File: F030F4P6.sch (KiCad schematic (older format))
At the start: 7 parts, among them U1 STM32F030F4P6, Y1 Crystal

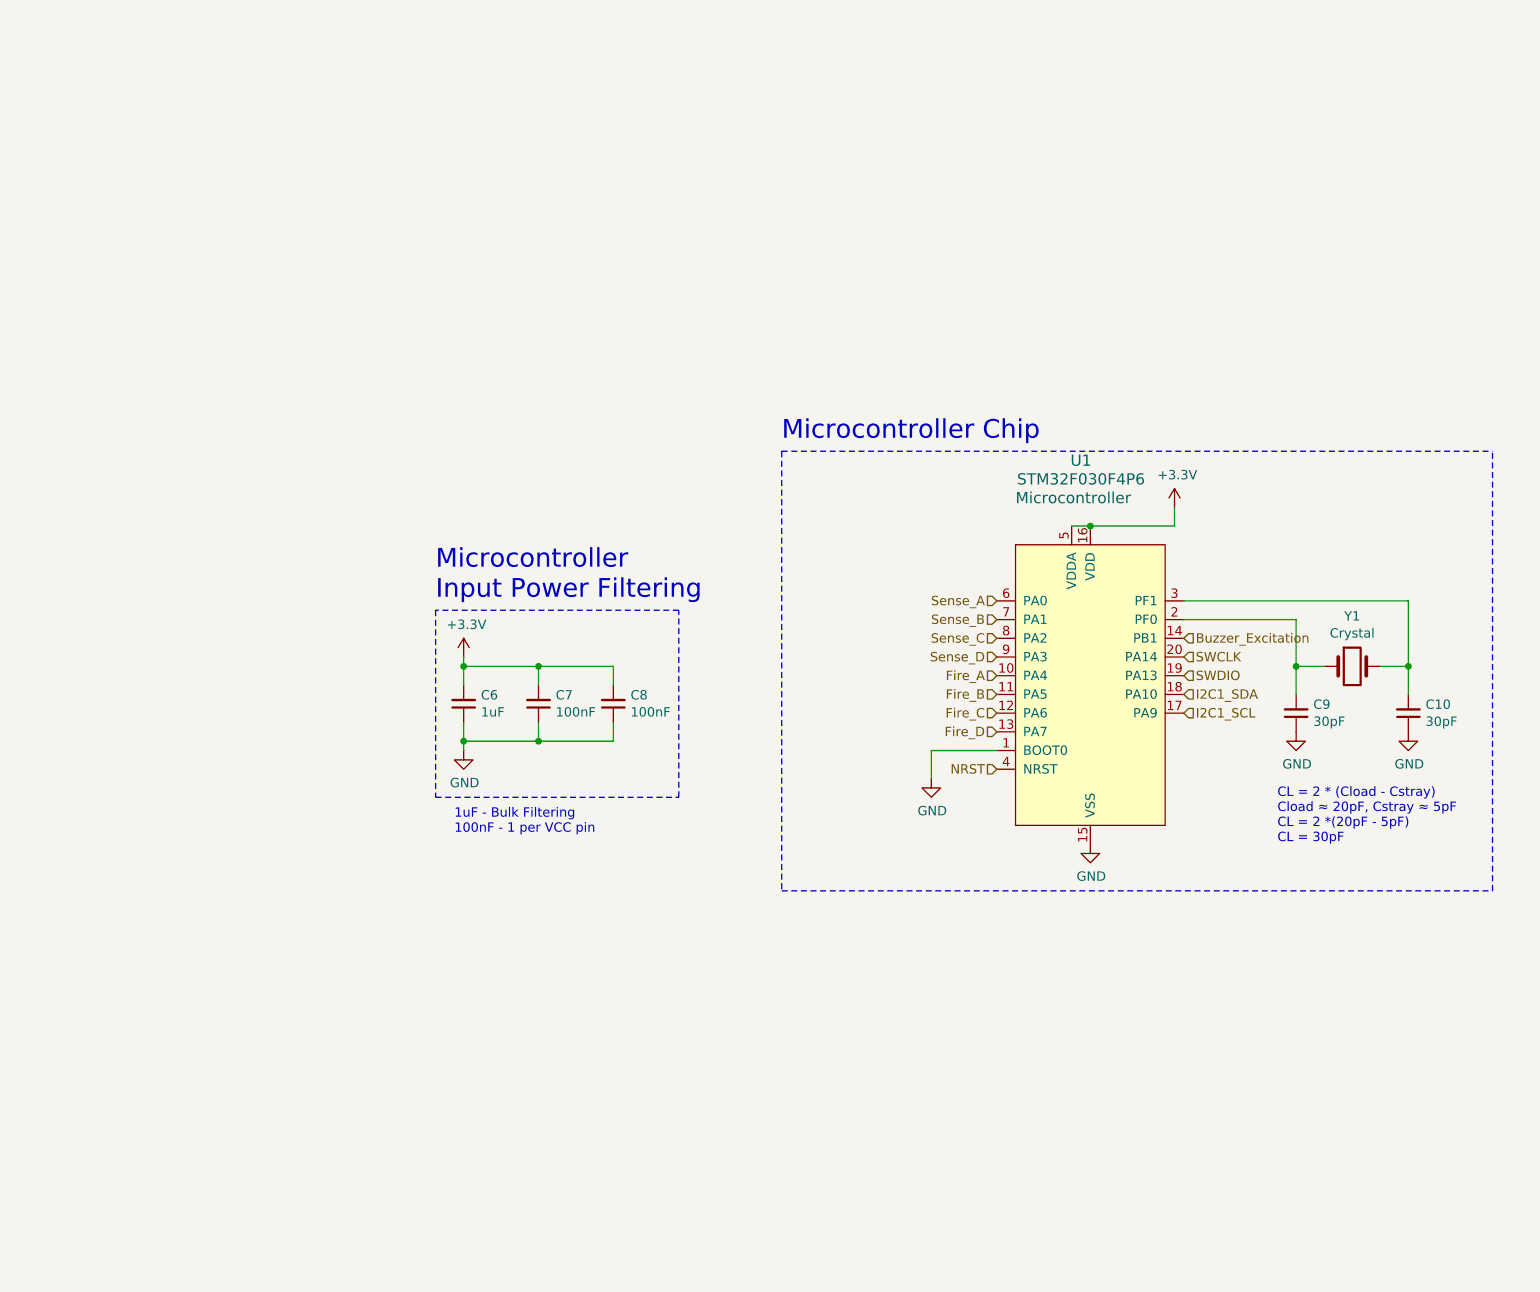
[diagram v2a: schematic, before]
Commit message: Updated PCB
Finalized most of the charges board and PCB
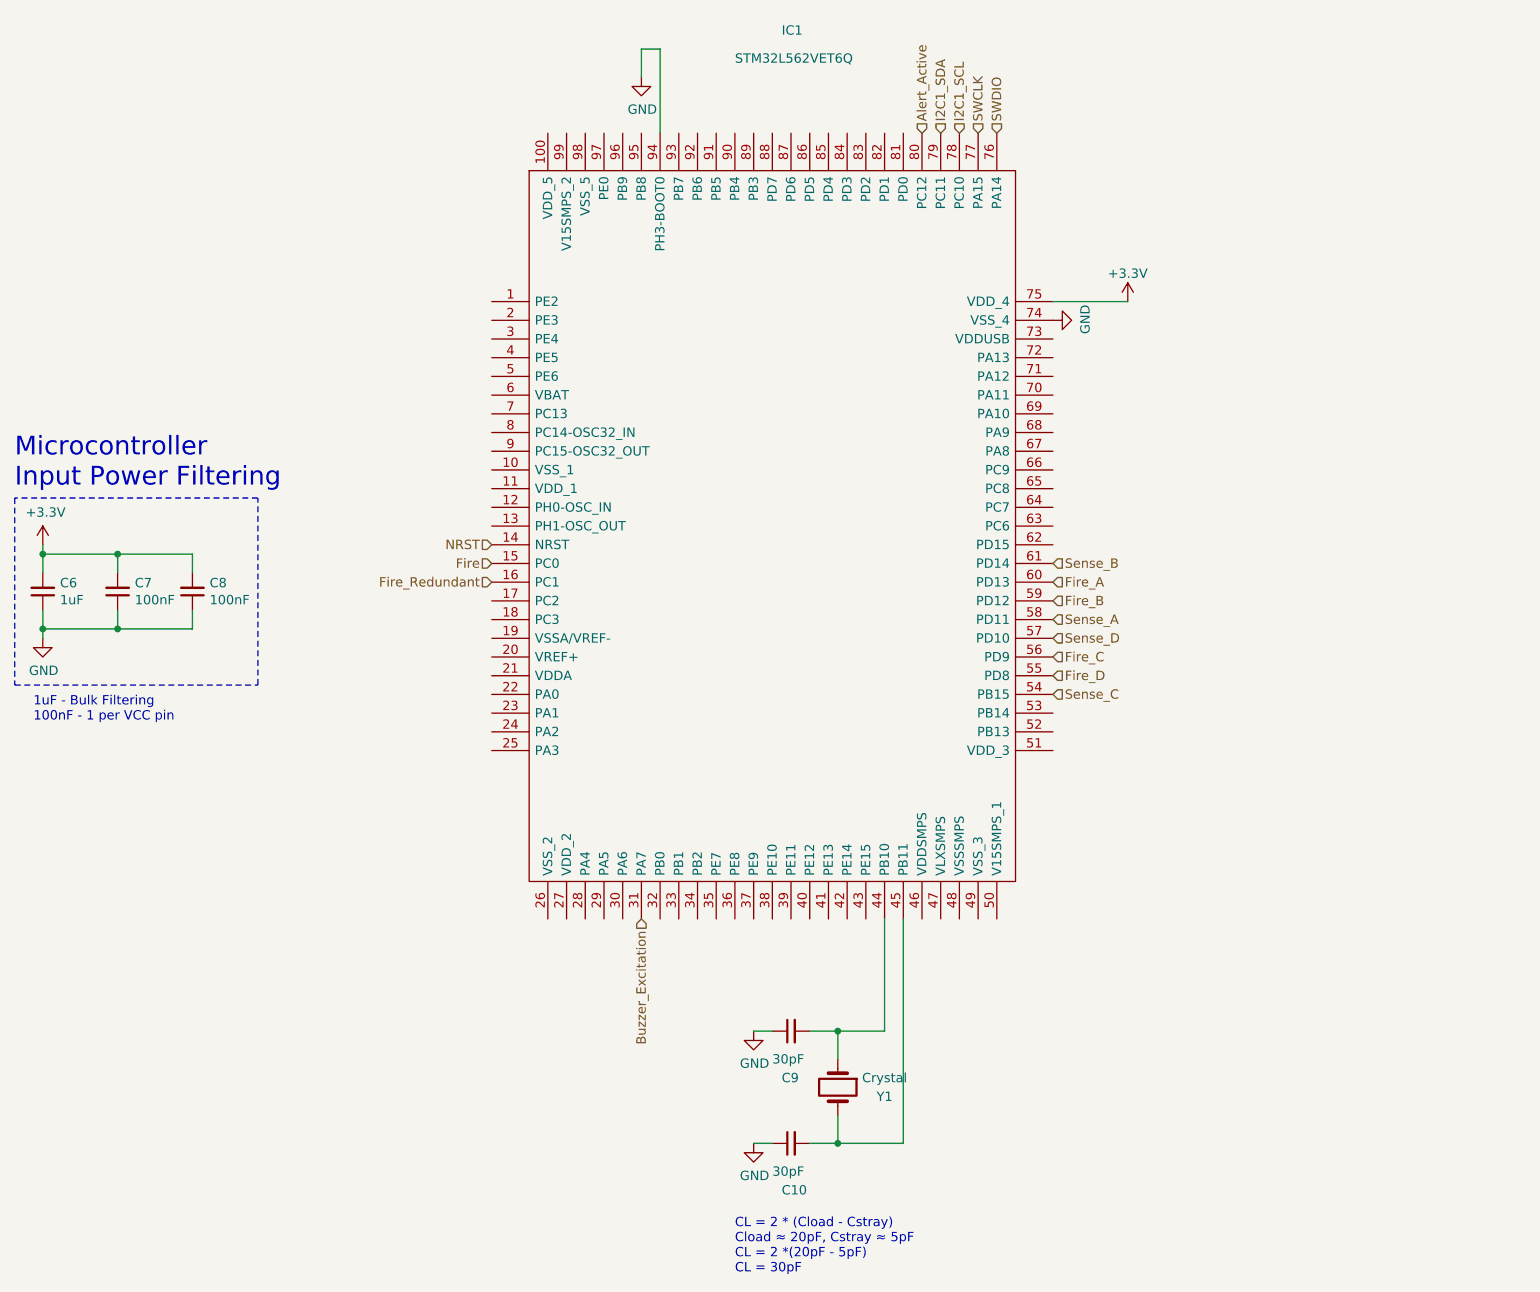
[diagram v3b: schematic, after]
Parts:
- removed U1: STM32F030F4P6, digikey-footprints:TSSOP-20_W4.4mm, symbol dk_Embedded-Microcontrollers:STM32F030F4P6
- added IC1: STM32L562VET6Q, SamacSys_Parts:QFP50P1600X1600X160-100N, symbol SamacSys_Parts:STM32L562VET6Q
- C10, C6, C7, C8, C9: footprint (none) -> Capacitor_SMD:C_0603_1608Metric
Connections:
- net +3V3: now also IC1.75 (VDD_4)
- net Buzzer_Excitation: now also IC1.31 (PA7)
- net Fire_A: now also IC1.60 (PD13)
- net Fire_B: now also IC1.59 (PD12)
- net Fire_C: now also IC1.56 (PD9)
- net Fire_D: now also IC1.55 (PD8)
- net GND: now also IC1.74 (VSS_4), IC1.94 (PH3-BOOT0)
- net I2C1_SCL: now also IC1.78 (PC10)
- net I2C1_SDA: now also IC1.79 (PC11)
- net NRST: now also IC1.14 (NRST)
- net SWCLK: now also IC1.77 (PA15)
- net SWDIO: now also IC1.76 (PA14)
- net Sense_A: now also IC1.58 (PD11)
- net Sense_B: now also IC1.61 (PD14)
- net Sense_C: now also IC1.54 (PB15)
- net Sense_D: now also IC1.57 (PD10)
- net at C9.2, Y1.1: now also IC1.44 (PB10)
- net at C10.2, Y1.2: now also IC1.45 (PB11)
- new net Alert_Active: IC1.80 (PC12)
- new net Fire: IC1.15 (PC0)
- new net Fire_Redundant: IC1.16 (PC1)
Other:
- note removed: "Microcontroller Chip"
- moved on the sheet: C10, C6, C7, C8, C9, Y1

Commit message: Fix to components
Changed the buzzer and terminal blocks
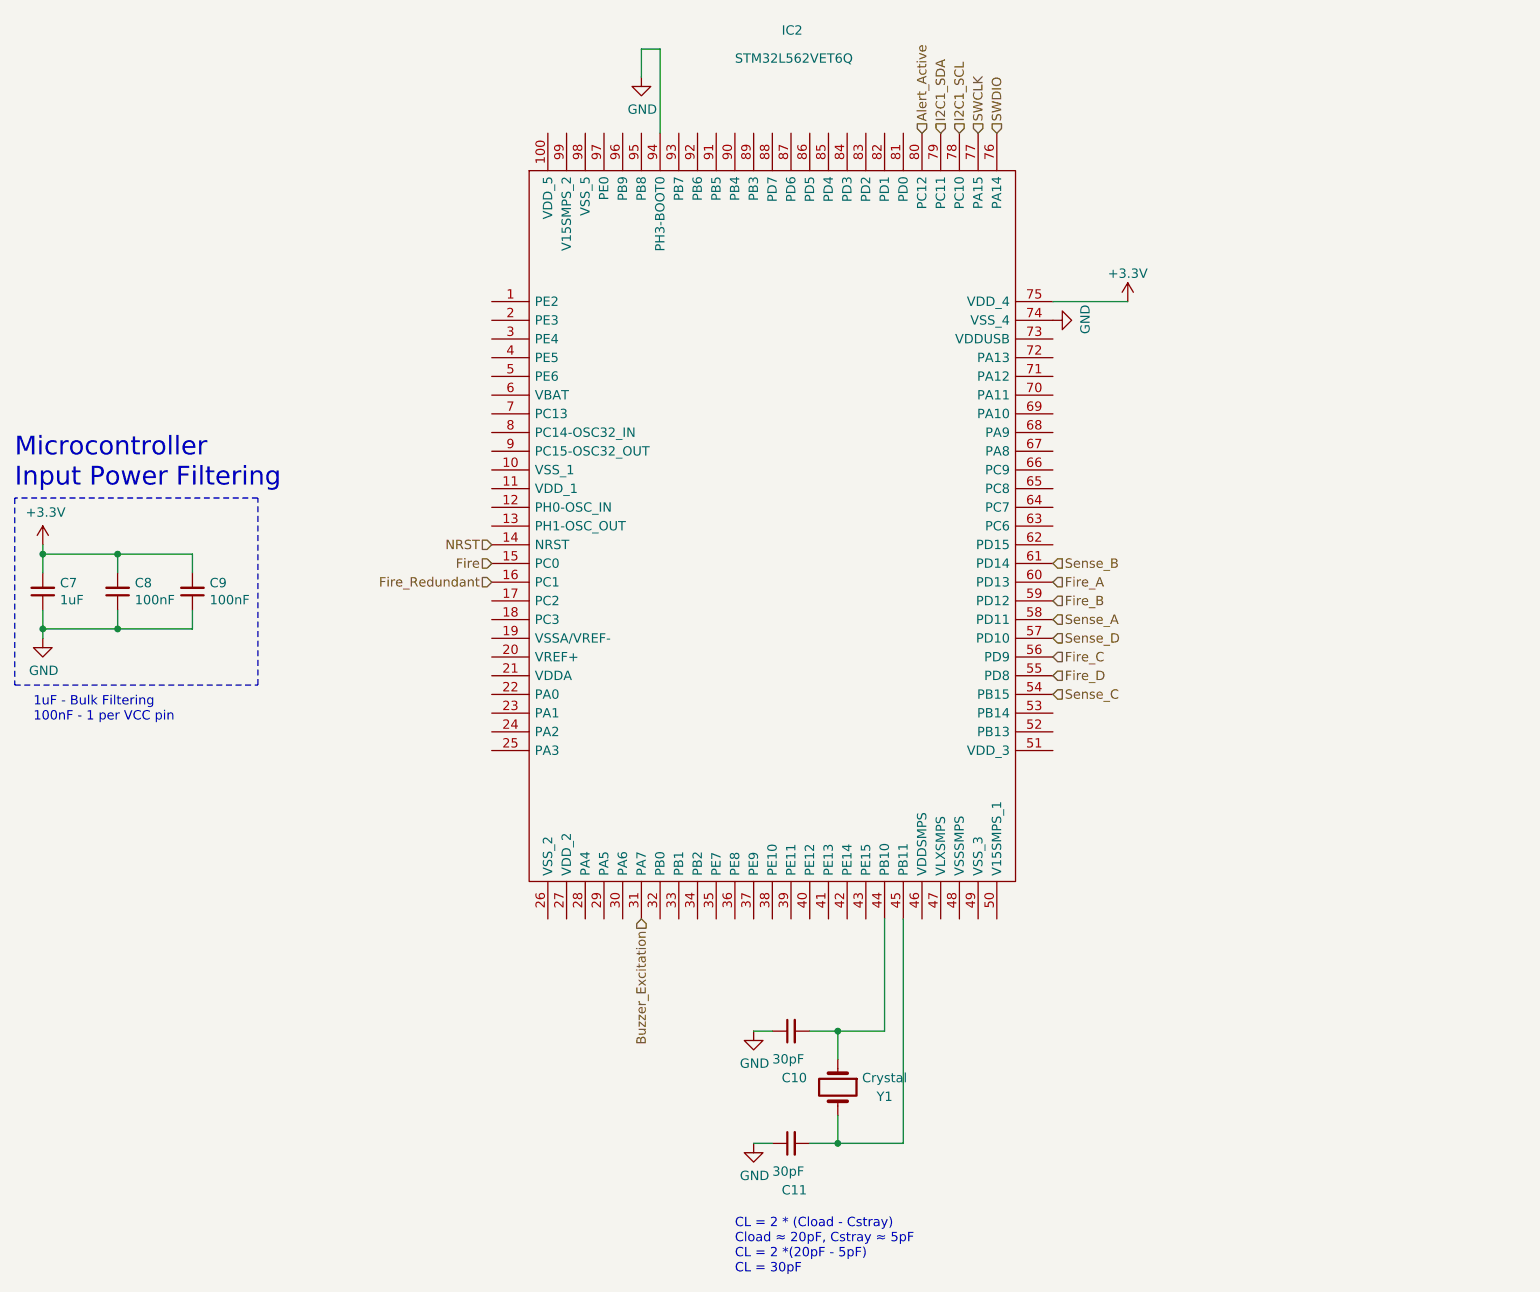
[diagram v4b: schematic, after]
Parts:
- renumbered C9 to C10, C10 to C11, C6 to C7, C7 to C8, C8 to C9, IC1 to IC2
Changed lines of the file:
@@
 P 5250 6700
 AR Path="/61614648" Ref="C?"  Part="1"
-AR Path="/6160DF75/61614648" Ref="C10"  Part="1"
-F 0 "C10" V 5000 6750 50  0000 R CNN
+AR Path="/6160DF75/61614648" Ref="C11"  Part="1"
+F 0 "C11" V 5000 6750 50  0000 R CNN
 F 1 "30pF" V 5100 6800 50  0000 R CNN
 F 2 "Capacitor_SMD:C_0603_1608Metric" H 5250 6700 50  0001 C CNN
@@
 P 5250 6100
 AR Path="/6161464E" Ref="C?"  Part="1"
-AR Path="/6160DF75/6161464E" Ref="C9"  Part="1"
-F 0 "C9" V 5000 6150 50  0000 R CNN
+AR Path="/6160DF75/6161464E" Ref="C10"  Part="1"
+F 0 "C10" V 5000 6150 50  0000 R CNN
 F 1 "30pF" V 5100 6200 50  0000 R CNN
 F 2 "Capacitor_SMD:C_0603_1608Metric" H 5250 6100 50  0001 C CNN
@@
 P 5050 6100
 AR Path="/61614655" Ref="#PWR?"  Part="1"
-AR Path="/6160DF75/61614655" Ref="#PWR037"  Part="1"
-F 0 "#PWR037" H 5050 5850 50  0001 C CNN
+AR Path="/6160DF75/61614655" Ref="#PWR035"  Part="1"
+F 0 "#PWR035" H 5050 5850 50  0001 C CNN
 F 1 "GND" H 5055 5927 50  0000 C CNN
 F 2 "" H 5050 6100 50  0001 C CNN
@@
 P 5050 6700
 AR Path="/6161465B" Ref="#PWR?"  Part="1"
-AR Path="/6160DF75/6161465B" Ref="#PWR038"  Part="1"
-F 0 "#PWR038" H 5050 6450 50  0001 C CNN
+AR Path="/6160DF75/6161465B" Ref="#PWR036"  Part="1"
+F 0 "#PWR036" H 5050 6450 50  0001 C CNN
 F 1 "GND" H 5055 6527 50  0000 C CNN
 F 2 "" H 5050 6700 50  0001 C CNN
@@
 P 1250 3750
 AR Path="/61614678" Ref="C?"  Part="1"
-AR Path="/6160DF75/61614678" Ref="C6"  Part="1"
-F 0 "C6" H 1158 3704 50  0000 R CNN
+AR Path="/6160DF75/61614678" Ref="C7"  Part="1"
+F 0 "C7" H 1158 3704 50  0000 R CNN
 F 1 "1uF" H 1158 3795 50  0000 R CNN
 F 2 "Capacitor_SMD:C_0603_1608Metric" H 1250 3750 50  0001 C CNN
@@
 P 1650 3750
 AR Path="/6161467E" Ref="C?"  Part="1"
-AR Path="/6160DF75/6161467E" Ref="C7"  Part="1"
-F 0 "C7" H 1558 3704 50  0000 R CNN
+AR Path="/6160DF75/6161467E" Ref="C8"  Part="1"
+F 0 "C8" H 1558 3704 50  0000 R CNN
 F 1 "100nF" H 1558 3795 50  0000 R CNN
 F 2 "Capacitor_SMD:C_0603_1608Metric" H 1650 3750 50  0001 C CNN
@@
 P 2050 3750
 AR Path="/61614684" Ref="C?"  Part="1"
-AR Path="/6160DF75/61614684" Ref="C8"  Part="1"
-F 0 "C8" H 1958 3704 50  0000 R CNN
+AR Path="/6160DF75/61614684" Ref="C9"  Part="1"
+F 0 "C9" H 1958 3704 50  0000 R CNN
 F 1 "100nF" H 1958 3795 50  0000 R CNN
 F 2 "Capacitor_SMD:C_0603_1608Metric" H 2050 3750 50  0001 C CNN
@@
 Wire Notes Line
 	1100 3250 1100 4250
-Text HLabel 6250 1300 1    50   Input ~ 0
-SWCLK
-Text HLabel 6350 1300 1    50   Input ~ 0
-SWDIO
 Text HLabel 6150 1300 1    50   Input ~ 0
 I2C1_SCL
@@
 I2C1_SDA
 $Comp
-L SamacSys_Parts:STM32L562VET6Q IC1
+L SamacSys_Parts:STM32L562VET6Q IC2
 U 1 1 61A3157F
 P 3650 2200
-F 0 "IC1" H 5200 3650 50  0000 L CNN
+F 0 "IC2" H 5200 3650 50  0000 L CNN
 F 1 "STM32L562VET6Q" H 4950 3500 50  0000 L CNN
 F 2 "SamacSys_Parts:QFP50P1600X1600X160-100N" H 6500 2900 50  0001 L CNN
@@
 P 6650 2300
 AR Path="/6161462F" Ref="#PWR?"  Part="1"
-AR Path="/6160DF75/6161462F" Ref="#PWR035"  Part="1"
-F 0 "#PWR035" H 6650 2050 50  0001 C CNN
+AR Path="/6160DF75/6161462F" Ref="#PWR037"  Part="1"
+F 0 "#PWR037" H 6650 2050 50  0001 C CNN
 F 1 "GND" H 6655 2127 50  0000 C CNN
 F 2 "" H 6650 2300 50  0001 C CNN
@@
 P 7050 2200
 AR Path="/6161463B" Ref="#PWR?"  Part="1"
-AR Path="/6160DF75/6161463B" Ref="#PWR036"  Part="1"
-F 0 "#PWR036" H 7050 2050 50  0001 C CNN
+AR Path="/6160DF75/6161463B" Ref="#PWR038"  Part="1"
+F 0 "#PWR038" H 7050 2050 50  0001 C CNN
 F 1 "+3.3V" H 7050 2350 50  0000 C CNN
 F 2 "" H 7050 2200 50  0001 C CNN
@@
 Text HLabel 6650 3900 2    50   Input ~ 0
 Sense_A
+Text HLabel 6250 1300 1    50   Input ~ 0
+SWCLK
+Text HLabel 6350 1300 1    50   Input ~ 0
+SWDIO
 $EndSCHEMATC

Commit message: updated board
updated the board again
added a crystal
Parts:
- Y1: value Crystal -> 32mhz; footprint (none) -> Crystal:Crystal_HC49-4H_Vertical
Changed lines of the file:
@@
 AR Path="/6160DF75/61614642" Ref="Y1"  Part="1"
 F 0 "Y1" V 5550 6650 50  0000 C CNN
-F 1 "Crystal" V 5450 6650 50  0000 C CNN
-F 2 "" H 5500 6400 50  0001 C CNN
+F 1 "32mhz" V 5450 6650 50  0000 C CNN
+F 2 "Crystal:Crystal_HC49-4H_Vertical" H 5500 6400 50  0001 C CNN
 F 3 "~" H 5500 6400 50  0001 C CNN
 	1    5500 6400
